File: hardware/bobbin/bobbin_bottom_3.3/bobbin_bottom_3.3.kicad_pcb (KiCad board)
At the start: 2 copper layers, 68.5 x 8.5 mm, 2 parts

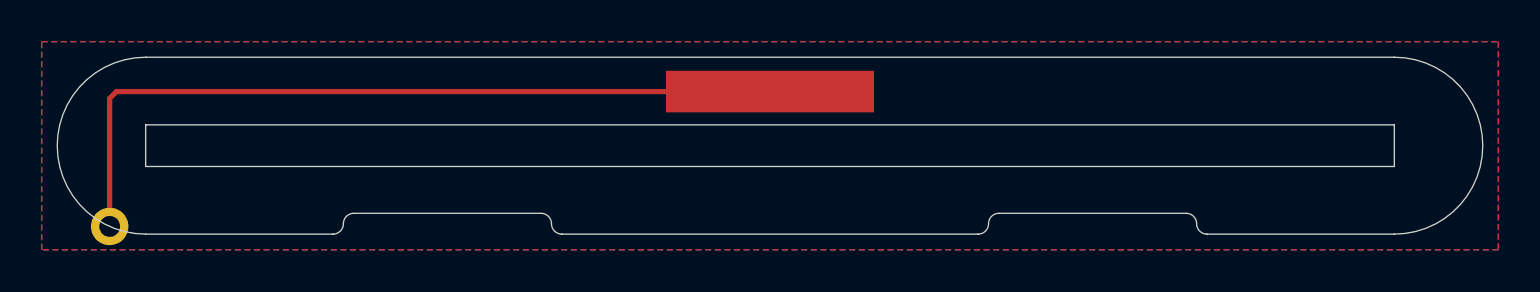
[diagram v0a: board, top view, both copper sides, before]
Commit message: Correct pad layers
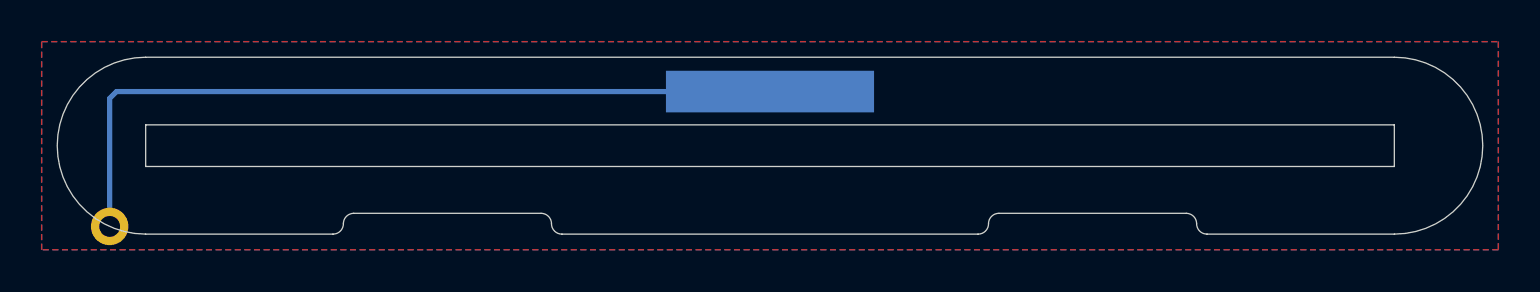
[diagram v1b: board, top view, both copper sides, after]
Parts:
- H4: moved to B.Cu
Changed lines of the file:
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@@
   (page A4)
   (layers
-    (0 F.Cu signal hide)
-    (31 B.Cu signal hide)
-    (32 B.Adhes user hide)
-    (33 F.Adhes user hide)
-    (34 B.Paste user hide)
-    (35 F.Paste user hide)
-    (36 B.SilkS user hide)
-    (37 F.SilkS user hide)
-    (38 B.Mask user hide)
-    (39 F.Mask user hide)
-    (40 Dwgs.User user hide)
-    (41 Cmts.User user hide)
-    (42 Eco1.User user hide)
-    (43 Eco2.User user hide)
+    (0 F.Cu signal)
+    (31 B.Cu signal)
+    (32 B.Adhes user)
+    (33 F.Adhes user)
+    (34 B.Paste user)
+    (35 F.Paste user)
+    (36 B.SilkS user)
+    (37 F.SilkS user)
+    (38 B.Mask user)
+    (39 F.Mask user)
+    (40 Dwgs.User user)
+    (41 Cmts.User user)
+    (42 Eco1.User user)
+    (43 Eco2.User user)
     (44 Edge.Cuts user)
-    (45 Margin user hide)
+    (45 Margin user)
     (46 B.CrtYd user hide)
     (47 F.CrtYd user hide)
@@
       (net 1 GND))
   )
-  (module cycfi_library:single-pad-10x2 (layer F.Cu)
+  (module cycfi_library:single-pad-10x2 (layer B.Cu)
     (at 130 98.4)
-    (fp_text reference H4 (at 3 0.6) (layer F.SilkS) hide
-      (effects (font (size 1 1) (thickness 0.15)))
+    (fp_text reference H4 (at 3 -0.6) (layer B.SilkS) hide
+      (effects (font (size 1 1) (thickness 0.15)) (justify mirror))
     )
-    (fp_text value "Core GND" (at 0 -2.54) (layer F.Fab)
-      (effects (font (size 1 1) (thickness 0.15)))
+    (fp_text value "Core GND" (at 0 2.54) (layer B.Fab)
+      (effects (font (size 1 1) (thickness 0.15)) (justify mirror))
     )
-    (pad 1 smd rect (at 0 0) (size 10 2) (layers F.Cu F.Paste F.Mask)
+    (pad 1 smd rect (at 0 0) (size 10 2) (layers B.Cu B.Paste B.Mask)
       (net 1 GND))
   )
@@
   (gr_arc (start 141 104.75) (end 141 104.25) (angle -90) (layer Edge.Cuts) (width 0.05))
   (gr_arc (start 140 104.75) (end 140 105.25) (angle -90) (layer Edge.Cuts) (width 0.05))
-  (segment (start 130 98.4) (end 98.6 98.4) (width 0.25) (layer F.Cu) (net 1))
+  (segment (start 130 98.4) (end 98.6 98.4) (width 0.25) (layer B.Cu) (net 1))
   (segment (start 98.27 104.517267) (end 98.361624 104.561143) (width 0.25) (layer F.Cu) (net 1))
-  (segment (start 98.27 98.73) (end 98.27 104.517267) (width 0.25) (layer F.Cu) (net 1))
-  (segment (start 98.6 98.4) (end 98.27 98.73) (width 0.25) (layer F.Cu) (net 1))
+  (segment (start 98.27 98.73) (end 98.27 104.517267) (width 0.25) (layer B.Cu) (net 1))
+  (segment (start 98.6 98.4) (end 98.27 98.73) (width 0.25) (layer B.Cu) (net 1))
   (zone (net 1) (net_name GND) (layer F.Cu) (hatch edge 0.508)
     (connect_pads yes (clearance 0.25))

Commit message: Preamp, Tone Block, Passive, and Bobbin Panel updates
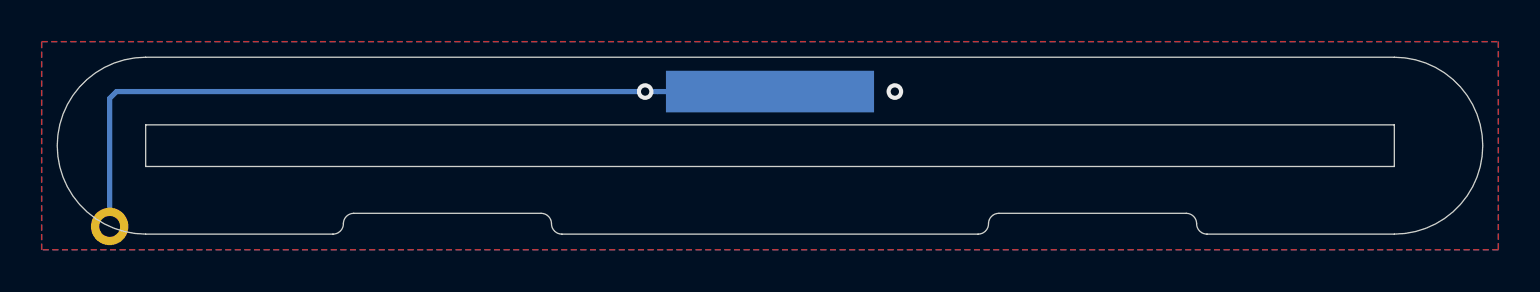
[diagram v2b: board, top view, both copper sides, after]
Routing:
- net GND: vias 0 -> 2
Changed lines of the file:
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@@
     (thickness 1.6)
     (drawings 52)
-    (tracks 4)
+    (tracks 7)
     (zones 0)
     (modules 2)
@@
   (gr_arc (start 141 104.75) (end 141 104.25) (angle -90) (layer Edge.Cuts) (width 0.05))
   (gr_arc (start 140 104.75) (end 140 105.25) (angle -90) (layer Edge.Cuts) (width 0.05))
-  (segment (start 130 98.4) (end 98.6 98.4) (width 0.25) (layer B.Cu) (net 1))
+  (segment (start 130 98.4) (end 124.6 98.4) (width 0.25) (layer B.Cu) (net 1))
   (segment (start 98.27 104.517267) (end 98.361624 104.561143) (width 0.25) (layer F.Cu) (net 1))
   (segment (start 98.27 98.73) (end 98.27 104.517267) (width 0.25) (layer B.Cu) (net 1))
   (segment (start 98.6 98.4) (end 98.27 98.73) (width 0.25) (layer B.Cu) (net 1))
+  (segment (start 124.6 98.4) (end 98.6 98.4) (width 0.25) (layer B.Cu) (net 1))
+  (via (at 124 98.4) (size 0.8) (drill 0.4) (layers F.Cu B.Cu) (net 1))
+  (via (at 136 98.4) (size 0.8) (drill 0.4) (layers F.Cu B.Cu) (net 1))
   (zone (net 1) (net_name GND) (layer F.Cu) (hatch edge 0.508)
     (connect_pads yes (clearance 0.25))

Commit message: Bobbin bottom new scheme
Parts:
- removed H3: single_pad_smd, cycfi_library:round-single-pad-1.8mm-th
- removed H4: Core GND, cycfi_library:single-pad-10x2
- added J1: Conn_01x01, cycfi_library:xr2-oc-coil-connector, F.Cu at (114.5, 105.2)
- added J2: Conn_01x03, cycfi_library:xr2-coil-connector, F.Cu at (114.5, 102.0)
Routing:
- net GND: track 37.8 -> 2.91 mm, vias 2 -> 1
- net /OC: track 0.00 -> 2.55 mm
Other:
- outline, holes or cut-outs redrawn
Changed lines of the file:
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@@
   (general
     (thickness 1.6)
-    (drawings 52)
-    (tracks 7)
+    (drawings 28)
+    (tracks 5)
     (zones 0)
     (modules 2)
-    (nets 2)
+    (nets 4)
   )
   (page A4)
@@
     (34 B.Paste user)
     (35 F.Paste user)
-    (36 B.SilkS user)
+    (36 B.SilkS user hide)
     (37 F.SilkS user)
     (38 B.Mask user)
     (39 F.Mask user)
-    (40 Dwgs.User user)
+    (40 Dwgs.User user hide)
     (41 Cmts.User user)
     (42 Eco1.User user)
@@
   (net 0 "")
   (net 1 GND)
+  (net 2 /OC)
+  (net 3 /IC)
   (net_class Default "This is the default net class."
     (clearance 0.2)
@@
     (uvia_dia 0.3)
     (uvia_drill 0.1)
+    (add_net /IC)
+    (add_net /OC)
     (add_net GND)
   )
-  (module cycfi_library:round-single-pad-1.8mm-th (layer F.Cu)
-    (at 98.27 104.88)
-    (fp_text reference H3 (at 2.73 -0.88) (layer F.SilkS) hide
+  (module cycfi_library:xr2-oc-coil-connector (layer F.Cu)
+    (at 114.5 105.2 180)
+    (fp_text reference J1 (at 0 5.08) (layer F.SilkS) hide
       (effects (font (size 1 1) (thickness 0.15)))
     )
-    (fp_text value single_pad_smd (at 0 -2.54) (layer F.Fab)
+    (fp_text value Conn_01x01 (at 0 -3.81) (layer F.Fab)
       (effects (font (size 1 1) (thickness 0.15)))
     )
-    (pad 1 thru_hole circle (at 0 0) (size 1.8 1.8) (drill 1) (layers *.Cu *.Mask)
-      (net 1 GND))
+    (pad 1 thru_hole circle (at 0 -0.05 180) (size 1.524 1.524) (drill 0.762) (layers *.Cu *.Mask)
+      (net 2 /OC))
   )
-  (module cycfi_library:single-pad-10x2 (layer B.Cu)
-    (at 130 98.4)
-    (fp_text reference H4 (at 3 -0.6) (layer B.SilkS) hide
+  (module cycfi_library:xr2-coil-connector (layer F.Cu)
+    (at 114.5 102)
+    (fp_text reference J2 (at 0 5.08) (layer F.SilkS) hide
+      (effects (font (size 1 1) (thickness 0.15)))
+    )
+    (fp_text value Conn_01x03 (at 0 -3.81) (layer F.Fab)
+      (effects (font (size 1 1) (thickness 0.15)))
+    )
+    (fp_text user IC (at 2.667 1.651 180) (layer F.SilkS)
+      (effects (font (size 1 1) (thickness 0.15)))
+    )
+    (fp_text user OC (at 0.127 1.651 180) (layer F.SilkS)
+      (effects (font (size 1 1) (thickness 0.15)))
+    )
+    (fp_text user GND (at -2.54 1.651 180) (layer F.SilkS)
+      (effects (font (size 1 1) (thickness 0.15)))
+    )
+    (fp_text user OC (at 0.127 1.651 180) (layer B.SilkS)
       (effects (font (size 1 1) (thickness 0.15)) (justify mirror))
     )
-    (fp_text value "Core GND" (at 0 2.54) (layer B.Fab)
+    (fp_text user GND (at -2.54 1.651 180) (layer B.SilkS)
       (effects (font (size 1 1) (thickness 0.15)) (justify mirror))
     )
-    (pad 1 smd rect (at 0 0) (size 10 2) (layers B.Cu B.Paste B.Mask)
+    (fp_text user IC (at 2.667 1.651 180) (layer B.SilkS)
+      (effects (font (size 1 1) (thickness 0.15)) (justify mirror))
+    )
+    (pad 1 thru_hole circle (at -2.54 0) (size 1.524 1.524) (drill 0.762) (layers *.Cu *.Mask)
       (net 1 GND))
+    (pad 2 thru_hole circle (at 0 0) (size 1.524 1.524) (drill 0.762) (layers *.Cu *.Mask)
+      (net 2 /OC))
+    (pad 3 thru_hole circle (at 2.54 0) (size 1.524 1.524) (drill 0.762) (layers *.Cu *.Mask)
+      (net 3 /IC))
   )
   (gr_line (start 100 102) (end 160 102) (layer Edge.Cuts) (width 0.05))
@@
   (gr_line (start 141 104.25) (end 150 104.25) (layer Dwgs.User) (width 0.05))
   (gr_line (start 120 105.25) (end 140 105.25) (layer Dwgs.User) (width 0.05))
-  (gr_line (start 135 99.399078) (end 135 97.399078) (layer Dwgs.User) (width 0.05))
   (gr_line (start 100 100) (end 160 100) (layer Dwgs.User) (width 0.05))
   (gr_line (start 160 100) (end 160 102) (layer Dwgs.User) (width 0.05))
   (gr_line (start 100 102) (end 160 102) (layer Dwgs.User) (width 0.05))
   (gr_line (start 100 100) (end 100 102) (layer Dwgs.User) (width 0.05))
-  (gr_line (start 125 99.399078) (end 125 97.399078) (layer Dwgs.User) (width 0.05))
-  (gr_line (start 125 97.399078) (end 135 97.399078) (layer Dwgs.User) (width 0.05))
   (gr_line (start 110 104.25) (end 119 104.25) (layer Dwgs.User) (width 0.05))
   (gr_line (start 100 105.25) (end 109 105.25) (layer Dwgs.User) (width 0.05))
   (gr_arc (start 151 104.75) (end 150.5 104.75) (angle -90) (layer Dwgs.User) (width 0.05))
-  (gr_line (start 125 99.399078) (end 135 99.399078) (layer Dwgs.User) (width 0.05))
-  (gr_line (start 125 97.399078) (end 135 99.399078) (layer Dwgs.User) (width 0.05))
-  (gr_line (start 125 99.399078) (end 135 97.399078) (layer Dwgs.User) (width 0.05))
-  (gr_line (start 135 99.399078) (end 135 97.399078) (layer Dwgs.User) (width 0.05))
   (gr_arc (start 140 104.75) (end 140 105.25) (angle -90) (layer Dwgs.User) (width 0.05))
   (gr_arc (start 109 104.75) (end 109 105.25) (angle -90) (layer Dwgs.User) (width 0.05))
   (gr_arc (start 150 104.75) (end 150.5 104.75) (angle -90) (layer Dwgs.User) (width 0.05))
   (gr_arc (start 141 104.75) (end 141 104.25) (angle -90) (layer Dwgs.User) (width 0.05))
-  (gr_line (start 125 97.399078) (end 135 97.399078) (layer Dwgs.User) (width 0.05))
-  (gr_line (start 125 99.399078) (end 125 97.399078) (layer Dwgs.User) (width 0.05))
-  (gr_line (start 125 99.399078) (end 135 99.399078) (layer Dwgs.User) (width 0.05))
-  (gr_arc (start 100 101) (end 98.739043 105.058631) (angle -17.25924264) (layer Dwgs.User) (width 0.05))
-  (gr_arc (start 98.269552 104.88665) (end 98.739043 105.058631) (angle -172.2370133) (layer Dwgs.User) (width 0.05))
   (gr_arc (start 160 101) (end 160 105.25) (angle -180) (layer Dwgs.User) (width 0.05))
-  (gr_arc (start 100 101) (end 100 96.75) (angle -149.2592426) (layer Dwgs.User) (width 0.05))
+  (gr_arc (start 100 101) (end 100 96.75) (angle -180) (layer Dwgs.User) (width 0.05))
   (gr_arc (start 110 104.75) (end 110 104.25) (angle -90) (layer Dwgs.User) (width 0.05))
   (gr_line (start 160 100) (end 160 102) (layer Edge.Cuts) (width 0.05))
-  (gr_line (start 110 104.25) (end 119 104.25) (layer Edge.Cuts) (width 0.05))
-  (gr_line (start 100 105.25) (end 109 105.25) (layer Edge.Cuts) (width 0.05))
-  (gr_line (start 151 105.25) (end 160 105.25) (layer Edge.Cuts) (width 0.05))
-  (gr_line (start 141 104.25) (end 150 104.25) (layer Edge.Cuts) (width 0.05))
-  (gr_line (start 120 105.25) (end 140 105.25) (layer Edge.Cuts) (width 0.05))
-  (gr_arc (start 120 104.75) (end 119.5 104.75) (angle -90) (layer Edge.Cuts) (width 0.05))
-  (gr_arc (start 119 104.75) (end 119.5 104.75) (angle -90) (layer Edge.Cuts) (width 0.05))
-  (gr_arc (start 110 104.75) (end 110 104.25) (angle -90) (layer Edge.Cuts) (width 0.05))
-  (gr_arc (start 109 104.75) (end 109 105.25) (angle -90) (layer Edge.Cuts) (width 0.05))
+  (gr_line (start 100 105.25) (end 160 105.25) (layer Edge.Cuts) (width 0.05))
   (gr_arc (start 160 101) (end 160 105.25) (angle -180) (layer Edge.Cuts) (width 0.05))
-  (gr_arc (start 151 104.75) (end 150.5 104.75) (angle -90) (layer Edge.Cuts) (width 0.05))
-  (gr_arc (start 150 104.75) (end 150.5 104.75) (angle -90) (layer Edge.Cuts) (width 0.05))
-  (gr_arc (start 141 104.75) (end 141 104.25) (angle -90) (layer Edge.Cuts) (width 0.05))
-  (gr_arc (start 140 104.75) (end 140 105.25) (angle -90) (layer Edge.Cuts) (width 0.05))
-  (segment (start 130 98.4) (end 124.6 98.4) (width 0.25) (layer B.Cu) (net 1))
-  (segment (start 98.27 104.517267) (end 98.361624 104.561143) (width 0.25) (layer F.Cu) (net 1))
-  (segment (start 98.27 98.73) (end 98.27 104.517267) (width 0.25) (layer B.Cu) (net 1))
-  (segment (start 98.6 98.4) (end 98.27 98.73) (width 0.25) (layer B.Cu) (net 1))
-  (segment (start 124.6 98.4) (end 98.6 98.4) (width 0.25) (layer B.Cu) (net 1))
-  (via (at 124 98.4) (size 0.8) (drill 0.4) (layers F.Cu B.Cu) (net 1))
-  (via (at 136 98.4) (size 0.8) (drill 0.4) (layers F.Cu B.Cu) (net 1))
+  (via (at 109.8 103.1) (size 0.8) (drill 0.4) (layers F.Cu B.Cu) (net 1))
+  (segment (start 111.96 103.1) (end 109.8 103.1) (width 0.25) (layer F.Cu) (net 1))
+  (segment (start 111.96 103.1) (end 111.96 102.35001) (width 0.25) (layer F.Cu) (net 1))
+  (segment (start 114.5 104.4) (end 114.5 104.89999) (width 0.25) (layer F.Cu) (net 2))
+  (segment (start 114.5 102.35001) (end 114.5 104.4) (width 0.25) (layer F.Cu) (net 2))
   (zone (net 1) (net_name GND) (layer F.Cu) (hatch edge 0.508)
-    (connect_pads yes (clearance 0.25))
+    (connect_pads (clearance 0.25))
     (min_thickness 0.254)
     (fill yes (arc_segments 32) (thermal_gap 0.508) (thermal_bridge_width 0.508))
@@
   )
   (zone (net 1) (net_name GND) (layer B.Cu) (hatch edge 0.508)
-    (connect_pads yes (clearance 0.25))
+    (connect_pads (clearance 0.25))
     (min_thickness 0.254)
     (fill yes (arc_segments 32) (thermal_gap 0.508) (thermal_bridge_width 0.508))

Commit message: updated drawing
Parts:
- moved J1 0.50 mm to (115.0, 105.2)
- moved J2 0.50 mm to (115.0, 102.0)
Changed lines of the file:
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@@
   (general
     (thickness 1.6)
-    (drawings 28)
+    (drawings 16)
     (tracks 5)
     (zones 0)
@@
     (34 B.Paste user)
     (35 F.Paste user)
-    (36 B.SilkS user hide)
+    (36 B.SilkS user)
     (37 F.SilkS user)
     (38 B.Mask user)
     (39 F.Mask user)
-    (40 Dwgs.User user hide)
+    (40 Dwgs.User user)
     (41 Cmts.User user)
     (42 Eco1.User user)
@@
     (44 Edge.Cuts user)
     (45 Margin user)
-    (46 B.CrtYd user hide)
-    (47 F.CrtYd user hide)
-    (48 B.Fab user hide)
-    (49 F.Fab user hide)
+    (46 B.CrtYd user)
+    (47 F.CrtYd user)
+    (48 B.Fab user)
+    (49 F.Fab user)
   )
   (setup
@@
   )
   (module cycfi_library:xr2-oc-coil-connector (layer F.Cu)
-    (at 114.5 105.2 180)
+    (at 115 105.2 180)
     (fp_text reference J1 (at 0 5.08) (layer F.SilkS) hide
       (effects (font (size 1 1) (thickness 0.15)))
@@
   )
   (module cycfi_library:xr2-coil-connector (layer F.Cu)
-    (at 114.5 102)
+    (at 115 102)
     (fp_text reference J2 (at 0 5.08) (layer F.SilkS) hide
       (effects (font (size 1 1) (thickness 0.15)))
@@
   (gr_arc (start 100 101) (end 100 96.75) (angle -180) (layer Edge.Cuts) (width 0.05))
   (gr_line (start 160 96.75) (end 100 96.75) (layer Edge.Cuts) (width 0.05))
-  (gr_arc (start 120 104.75) (end 119.5 104.75) (angle -90) (layer Dwgs.User) (width 0.05))
-  (gr_arc (start 119 104.75) (end 119.5 104.75) (angle -90) (layer Dwgs.User) (width 0.05))
   (gr_line (start 160 96.75) (end 100 96.75) (layer Dwgs.User) (width 0.05))
-  (gr_line (start 151 105.25) (end 160 105.25) (layer Dwgs.User) (width 0.05))
-  (gr_line (start 141 104.25) (end 150 104.25) (layer Dwgs.User) (width 0.05))
-  (gr_line (start 120 105.25) (end 140 105.25) (layer Dwgs.User) (width 0.05))
+  (gr_line (start 100 105.25) (end 160 105.25) (layer Dwgs.User) (width 0.05))
   (gr_line (start 100 100) (end 160 100) (layer Dwgs.User) (width 0.05))
   (gr_line (start 160 100) (end 160 102) (layer Dwgs.User) (width 0.05))
   (gr_line (start 100 102) (end 160 102) (layer Dwgs.User) (width 0.05))
   (gr_line (start 100 100) (end 100 102) (layer Dwgs.User) (width 0.05))
-  (gr_line (start 110 104.25) (end 119 104.25) (layer Dwgs.User) (width 0.05))
-  (gr_line (start 100 105.25) (end 109 105.25) (layer Dwgs.User) (width 0.05))
-  (gr_arc (start 151 104.75) (end 150.5 104.75) (angle -90) (layer Dwgs.User) (width 0.05))
-  (gr_arc (start 140 104.75) (end 140 105.25) (angle -90) (layer Dwgs.User) (width 0.05))
-  (gr_arc (start 109 104.75) (end 109 105.25) (angle -90) (layer Dwgs.User) (width 0.05))
-  (gr_arc (start 150 104.75) (end 150.5 104.75) (angle -90) (layer Dwgs.User) (width 0.05))
-  (gr_arc (start 141 104.75) (end 141 104.25) (angle -90) (layer Dwgs.User) (width 0.05))
   (gr_arc (start 160 101) (end 160 105.25) (angle -180) (layer Dwgs.User) (width 0.05))
   (gr_arc (start 100 101) (end 100 96.75) (angle -180) (layer Dwgs.User) (width 0.05))
-  (gr_arc (start 110 104.75) (end 110 104.25) (angle -90) (layer Dwgs.User) (width 0.05))
   (gr_line (start 160 100) (end 160 102) (layer Edge.Cuts) (width 0.05))
   (gr_line (start 100 105.25) (end 160 105.25) (layer Edge.Cuts) (width 0.05))
   (gr_arc (start 160 101) (end 160 105.25) (angle -180) (layer Edge.Cuts) (width 0.05))
-  (via (at 109.8 103.1) (size 0.8) (drill 0.4) (layers F.Cu B.Cu) (net 1))
-  (segment (start 111.96 103.1) (end 109.8 103.1) (width 0.25) (layer F.Cu) (net 1))
-  (segment (start 111.96 103.1) (end 111.96 102.35001) (width 0.25) (layer F.Cu) (net 1))
-  (segment (start 114.5 104.4) (end 114.5 104.89999) (width 0.25) (layer F.Cu) (net 2))
-  (segment (start 114.5 102.35001) (end 114.5 104.4) (width 0.25) (layer F.Cu) (net 2))
+  (via (at 110.3 103.1) (size 0.8) (drill 0.4) (layers F.Cu B.Cu) (net 1))
+  (segment (start 112.46 103.1) (end 110.3 103.1) (width 0.25) (layer F.Cu) (net 1))
+  (segment (start 112.46 103.1) (end 112.46 102.35001) (width 0.25) (layer F.Cu) (net 1))
+  (segment (start 115 104.4) (end 115 104.89999) (width 0.25) (layer F.Cu) (net 2))
+  (segment (start 115 102.35001) (end 115 104.4) (width 0.25) (layer F.Cu) (net 2))
   (zone (net 1) (net_name GND) (layer F.Cu) (hatch edge 0.508)
     (connect_pads (clearance 0.25))

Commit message: Upgrade to KiCad 6
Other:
- net class Default removed

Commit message: First shot v2 bobbin for 3.3"
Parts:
- added H1: single_pad, xr_spectra_library:rail_slot_3.3, F.Cu at (129.8, 101.0)
- added J3: IC, cycfi_library:single-pad-1.52x1.52-th, F.Cu at (96.5, 103.4)
- added J4: IC, cycfi_library:single-pad-1.52x1.52-th, F.Cu at (112.5, 105.2)
- J1: value Conn_01x01 -> OC; footprint cycfi_library:xr2-oc-coil-connector -> cycfi_library:single-pad-1.52x1.52-th
- J2: value Conn_01x03 -> OC; footprint cycfi_library:xr2-coil-connector -> cycfi_library:single-pad-1.52x1.52-th
- moved J2 48.5 mm to (163.5, 103.4), turned to 180 degrees
- moved J1 2.54 mm to (117.5, 105.2)
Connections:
- J2 pad 1: GND -> /OC
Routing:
- net /OC: track 2.55 -> 46.7 mm
- net /IC: track 0.00 -> 16.7 mm
- net GND: track 2.91 -> 0.00 mm, vias 1 -> 3
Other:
- outline, holes or cut-outs redrawn

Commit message: 3.5" and 4.0" bottom bobbin PCB layout
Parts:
- moved H1 0.25 mm to (130.0, 101.0)
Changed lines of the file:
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@@
   )
   (footprint "xr_spectra_library:rail_slot_3.3" (layer "F.Cu")
-    (at 129.75 101)
+    (at 130 101)
     (property "Sheetfile" "bobbin_bottom_3.3.kicad_sch")
     (property "Sheetname" "")
@@
       (effects (font (size 1 1) (thickness 0.15)))
     )
-    (pad "1" thru_hole oval (at 0.25 0) (size 61.2 2.2) (drill oval 61 2) (layers *.Cu *.Mask)
+    (pad "1" thru_hole oval (at 0 0) (size 61.2 2.2) (drill oval 61 2) (layers *.Cu *.Mask)
       (net 1 "GND") (pinfunction "1") (pintype "input"))
   )
@@
   (gr_line (start 141 104.85) (end 141 104.65) (layer "Dwgs.User") (width 0.01))
   (gr_line (start 160 100) (end 160 102) (layer "Dwgs.User") (width 0.01))
-  (gr_arc (start 96.125734 102.747159) (mid 97.12753 102.97865) (end 96.986778 103.997164) (layer "Dwgs.User") (width 0.01))
+  (gr_arc (start 96.125734 102.747159) (mid 97.12753 102.978649) (end 96.986778 103.997164) (layer "Dwgs.User") (width 0.01))
   (gr_line (start 100 100) (end 160 100) (layer "Dwgs.User") (width 0.01))
   (gr_arc (start 141 104.85) (mid 140.882843 105.132843) (end 140.6 105.25) (layer "Dwgs.User") (width 0.01))
   (gr_line (start 140.6 105.25) (end 100 105.25) (layer "Dwgs.User") (width 0.01))
-  (gr_arc (start 163.013222 103.997164) (mid 162.872471 102.978651) (end 163.874266 102.747159) (layer "Dwgs.User") (width 0.01))
+  (gr_arc (start 163.013222 103.997164) (mid 162.872472 102.97865) (end 163.874266 102.747159) (layer "Dwgs.User") (width 0.01))
   (gr_arc (start 100 105.25) (mid 95.75 101) (end 100 96.75) (layer "Dwgs.User") (width 0.01))
   (gr_line (start 141.4 104.25) (end 148.6 104.25) (layer "Dwgs.User") (width 0.01))
